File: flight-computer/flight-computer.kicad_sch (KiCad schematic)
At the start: 31 parts, among them J1 Conn_01x06_Pin, J2 Conn_01x06_Pin, J3 Power Connector, J4 Micro_SD_Card, J5 USB_C_Receptacle_USB2.0_16P, J6 Conn_01x02_Pin, Q1 DMN3404L, Q2 DMN3404L, SW3 SW_DIP_x02, U1 LMR51420X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

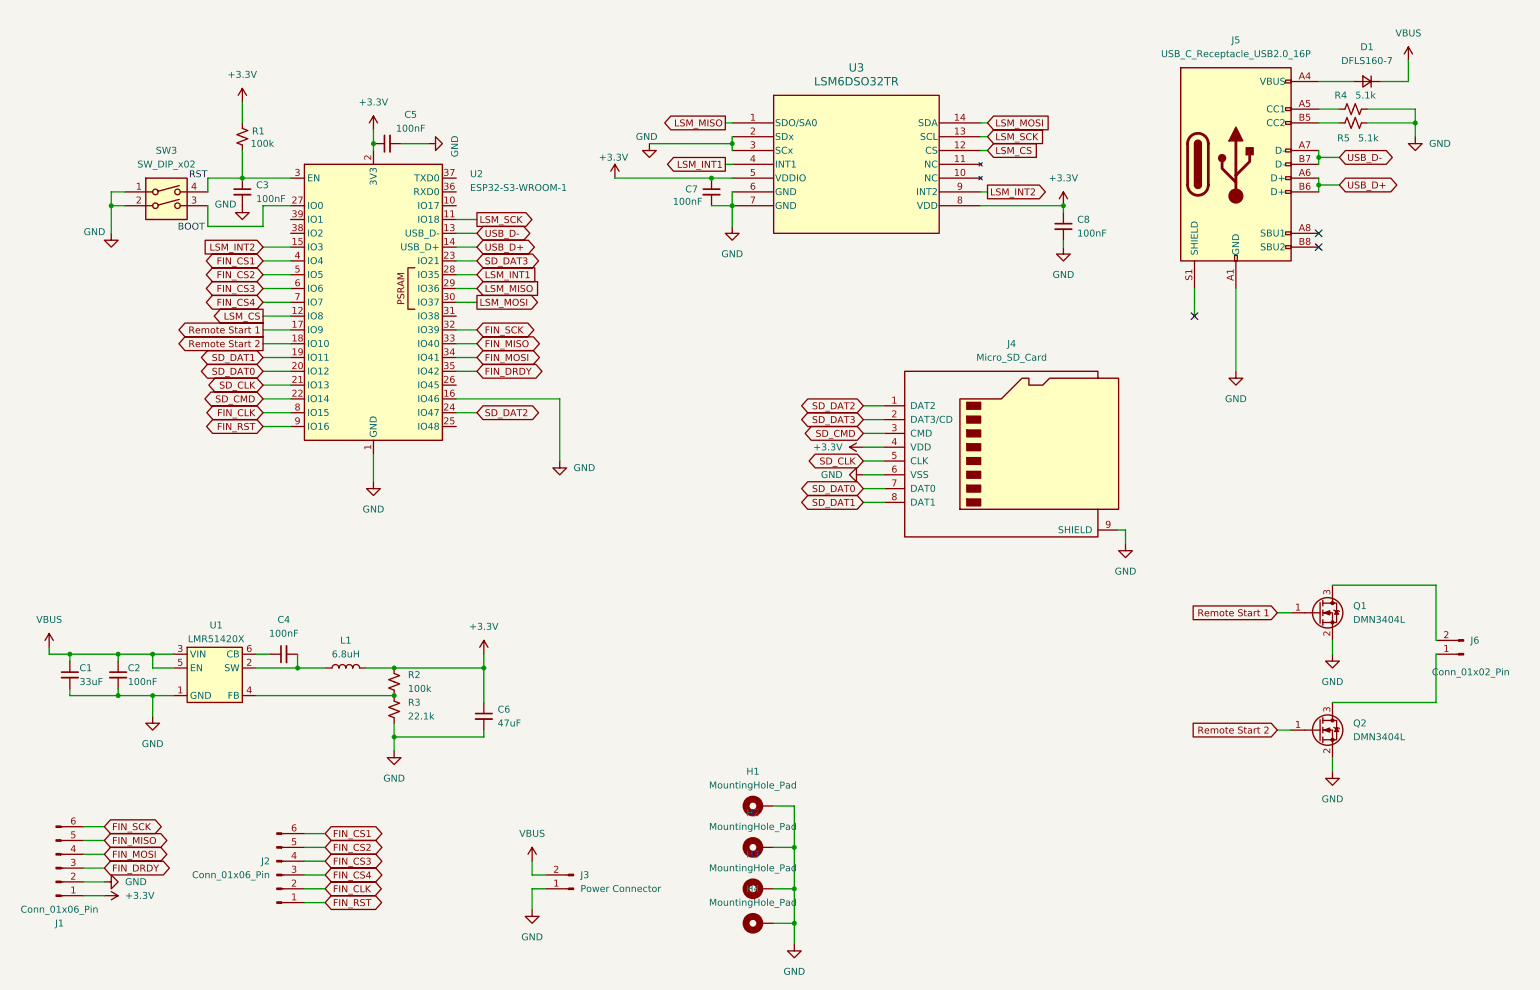
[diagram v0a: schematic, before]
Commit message: added current sensor stuff and rerouted fc
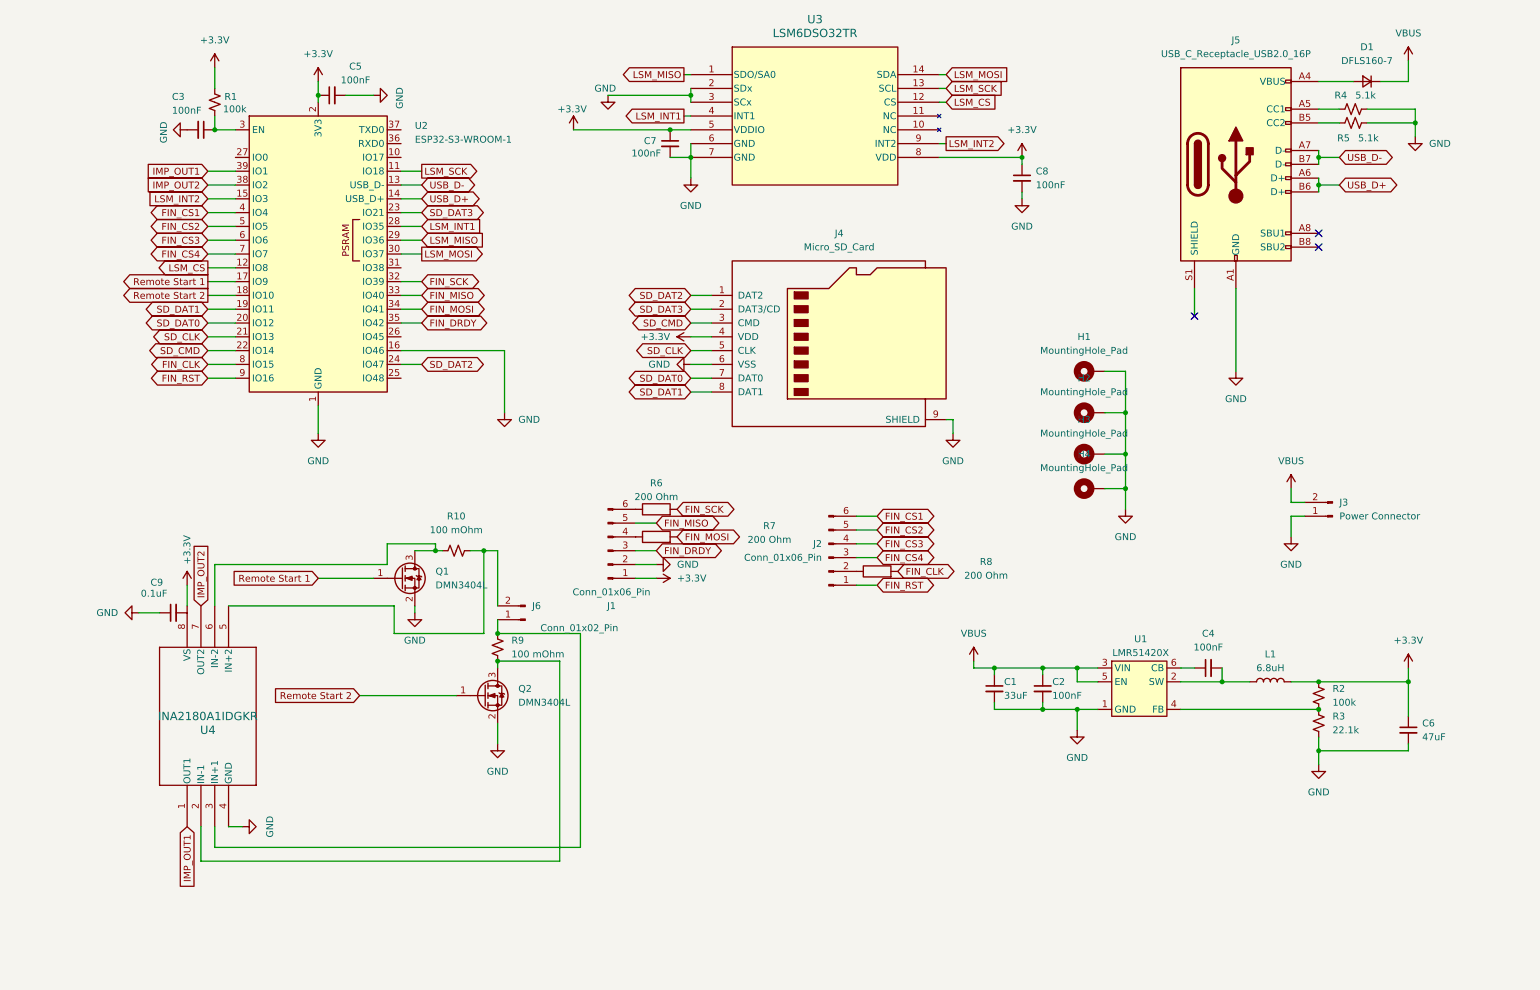
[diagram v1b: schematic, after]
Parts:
- removed SW3: SW_DIP_x02, Library:218-2LPSTR_CTS, symbol Switch:SW_DIP_x02
- added C9: 0.1uF, Capacitor_SMD:C_0402_1005Metric, symbol Device:C_Small
- added R10, R9: 100 mOhm, Resistor_SMD:R_0402_1005Metric, symbol Device:R_Small_US
- added R6, R7, R8: 200 Ohm, Resistor_SMD:R_0402_1005Metric, symbol Device:R
- added U4: INA2180A1IDGKR, Library:DGK8_TEX-M, symbol My_Library:INA2180A1IDGKR
- J3, J6: footprint Connector_PinHeader_2.54mm:PinHeader_1x02_P2.54mm_Vertical -> Library:CONN2_282834-2_TEC
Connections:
- net +3.3V: now also U4.8 (VS)
- net FIN_CLK: now also R8.2; no longer J2.2 (Pin_2)
- net FIN_MOSI: now also R7.2; no longer J1.4 (Pin_4)
- net FIN_SCK: now also R6.2; no longer J1.6 (Pin_6)
- net GND: now also C9.1, U4.4 (GND)
- net at Q1.3 (D): now also R10.1, U4.6 (IN-2); no longer J6.2 (Pin_2)
- net at J6.1 (Pin_1): now also R9.1, U4.3 (IN+1); no longer Q2.3 (D)
- net IMP_OUT2: now reaches U2.38 (IO2)
- net IMP_OUT2: now also U4.7 (OUT2)
- net IMP_OUT1: now reaches U2.39 (IO1)
- net IMP_OUT1: now also U4.1 (OUT1)
- new net: J2.2 (Pin_2), R8.1
- new net: J6.2 (Pin_2), R10.2, U4.5 (IN+2)
- new net: J1.4 (Pin_4), R7.1
- new net: J1.6 (Pin_6), R6.1
- new net: Q2.3 (D), R9.2, U4.2 (IN-1)
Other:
- note removed: "BOOT"
- note removed: "RST"
- moved on the sheet: C1, C2, C3, C4, C5, C6, C7, C8, H1, H2, H3, H4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

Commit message: finished connecting things
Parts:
- added R11, R12, R13, R14, R15: 200 Ohm, Resistor_SMD:R_0402_1005Metric, symbol Device:R
- J1, J2: footprint Connector_JST:JST_ZH_S6B-ZR-SM4A-TF_1x06-1MP_P1.50mm_Horizontal -> Connector_JST:JST_ZE_S06B-ZESK-2D_1x06_P1.50mm_Horizontal
- R10, R9: footprint Resistor_SMD:R_0402_1005Metric -> Resistor_SMD:R_1206_3216Metric
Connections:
- net +3.3V: now also C9.2
- net FIN_CS1: now also R12.2; no longer J2.6 (Pin_6)
- net FIN_CS2: now also R13.2; no longer J2.5 (Pin_5)
- net FIN_CS3: now also R14.2; no longer J2.4 (Pin_4)
- net FIN_CS4: now also R15.2; no longer J2.3 (Pin_3)
- net FIN_MISO: now also R11.2; no longer J1.5 (Pin_5)
- new net: J1.5 (Pin_5), R11.1
- new net: J2.3 (Pin_3), R15.1
- new net: J2.4 (Pin_4), R14.1
- new net: J2.5 (Pin_5), R13.1
- new net: J2.6 (Pin_6), R12.1
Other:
- moved on the sheet: C9

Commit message: started organizing
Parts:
- J1, J2: footprint Connector_JST:JST_ZE_S06B-ZESK-2D_1x06_P1.50mm_Horizontal -> Connector_JST:JST_ZE_SM06B-ZESS-TB_1x06-1MP_P1.50mm_Horizontal
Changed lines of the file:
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@@
 			)
 		)
-		(property "Footprint" "Connector_JST:JST_ZE_S06B-ZESK-2D_1x06_P1.50mm_Horizontal"
+		(property "Footprint" "Connector_JST:JST_ZE_SM06B-ZESS-TB_1x06-1MP_P1.50mm_Horizontal"
 			(at 163.83 116.84 0)
 			(effects
@@
 			)
 		)
-		(property "Footprint" "Connector_JST:JST_ZE_S06B-ZESK-2D_1x06_P1.50mm_Horizontal"
+		(property "Footprint" "Connector_JST:JST_ZE_SM06B-ZESS-TB_1x06-1MP_P1.50mm_Horizontal"
 			(at 123.19 115.57 0)
 			(effects
